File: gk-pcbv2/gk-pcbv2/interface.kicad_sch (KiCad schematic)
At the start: 69 parts, among them J11 Conn_01x02, J7 Conn_01x02, Q1 MMBT3904, Q2 MMBT3904, SW3 RotaryEncoder_Switch, SW4 SW_DIP_x01, U9 LSM6DSL

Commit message: more pcb changes
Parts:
- added J13: Conn_01x02, Connector_PinHeader_2.54mm:PinHeader_1x02_P2.54mm_Vertical, symbol Connector_Generic:Conn_01x02
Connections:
- net I2C4_SCL: now also J13.2 (Pin_2)
- net I2C4_SDA: now also J13.1 (Pin_1)

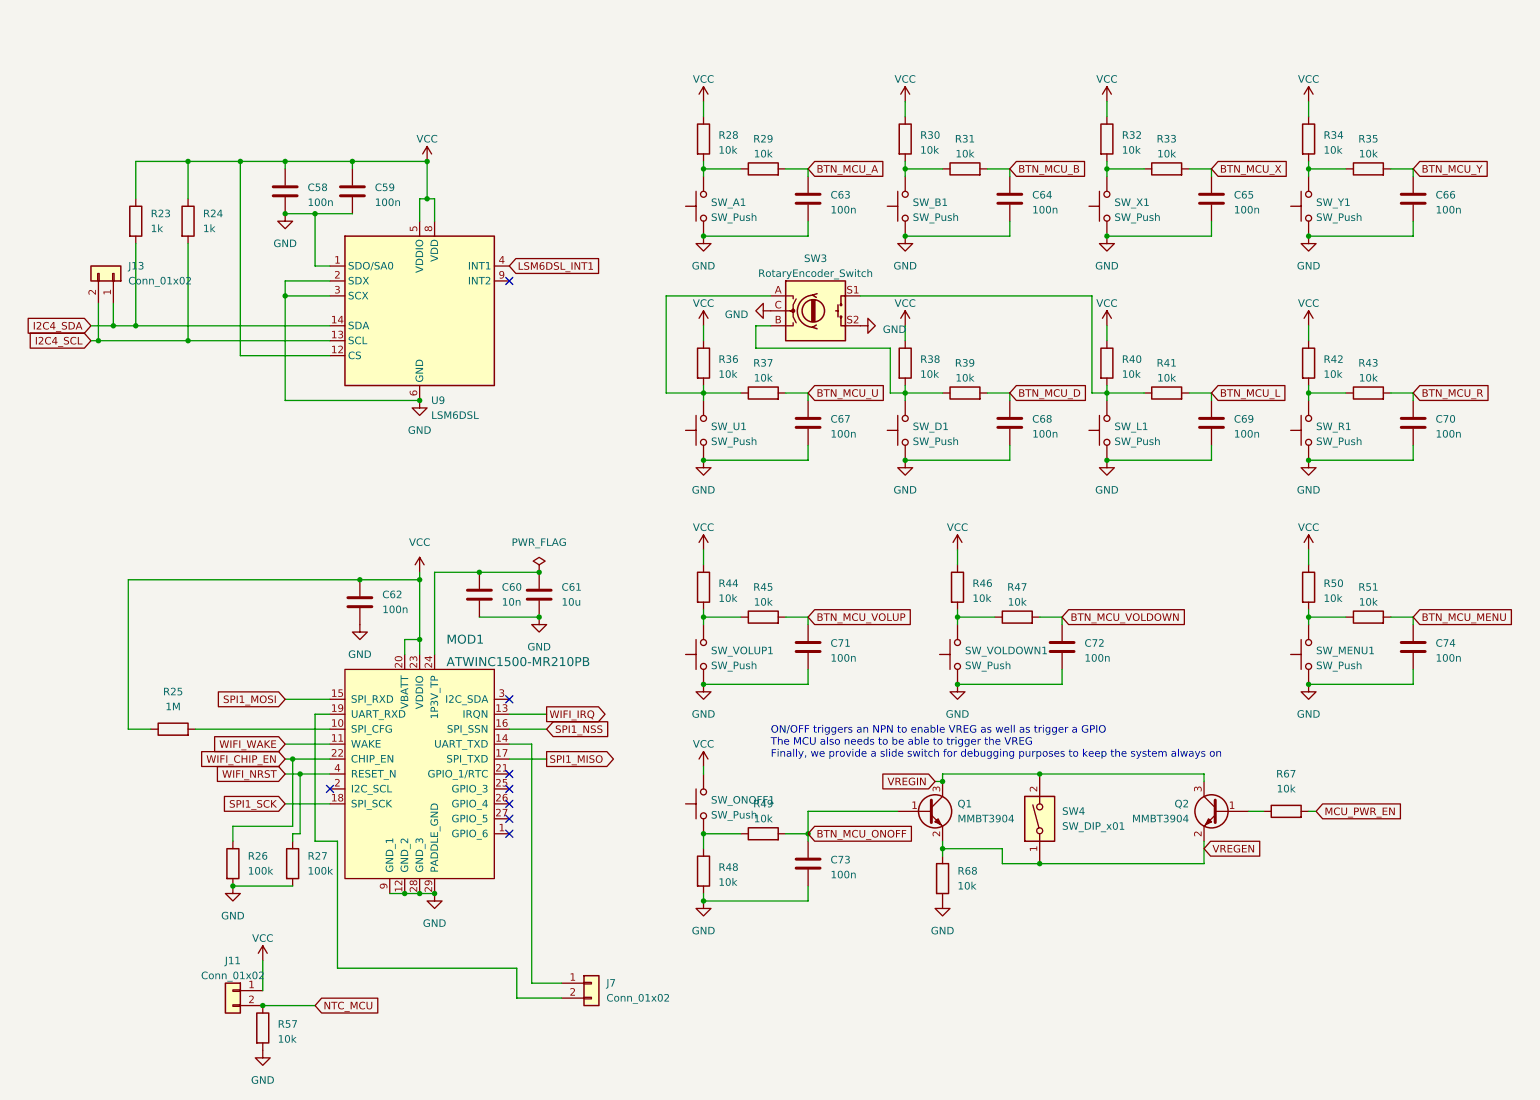
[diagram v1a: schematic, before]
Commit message: PCB updates - add xbox joystick
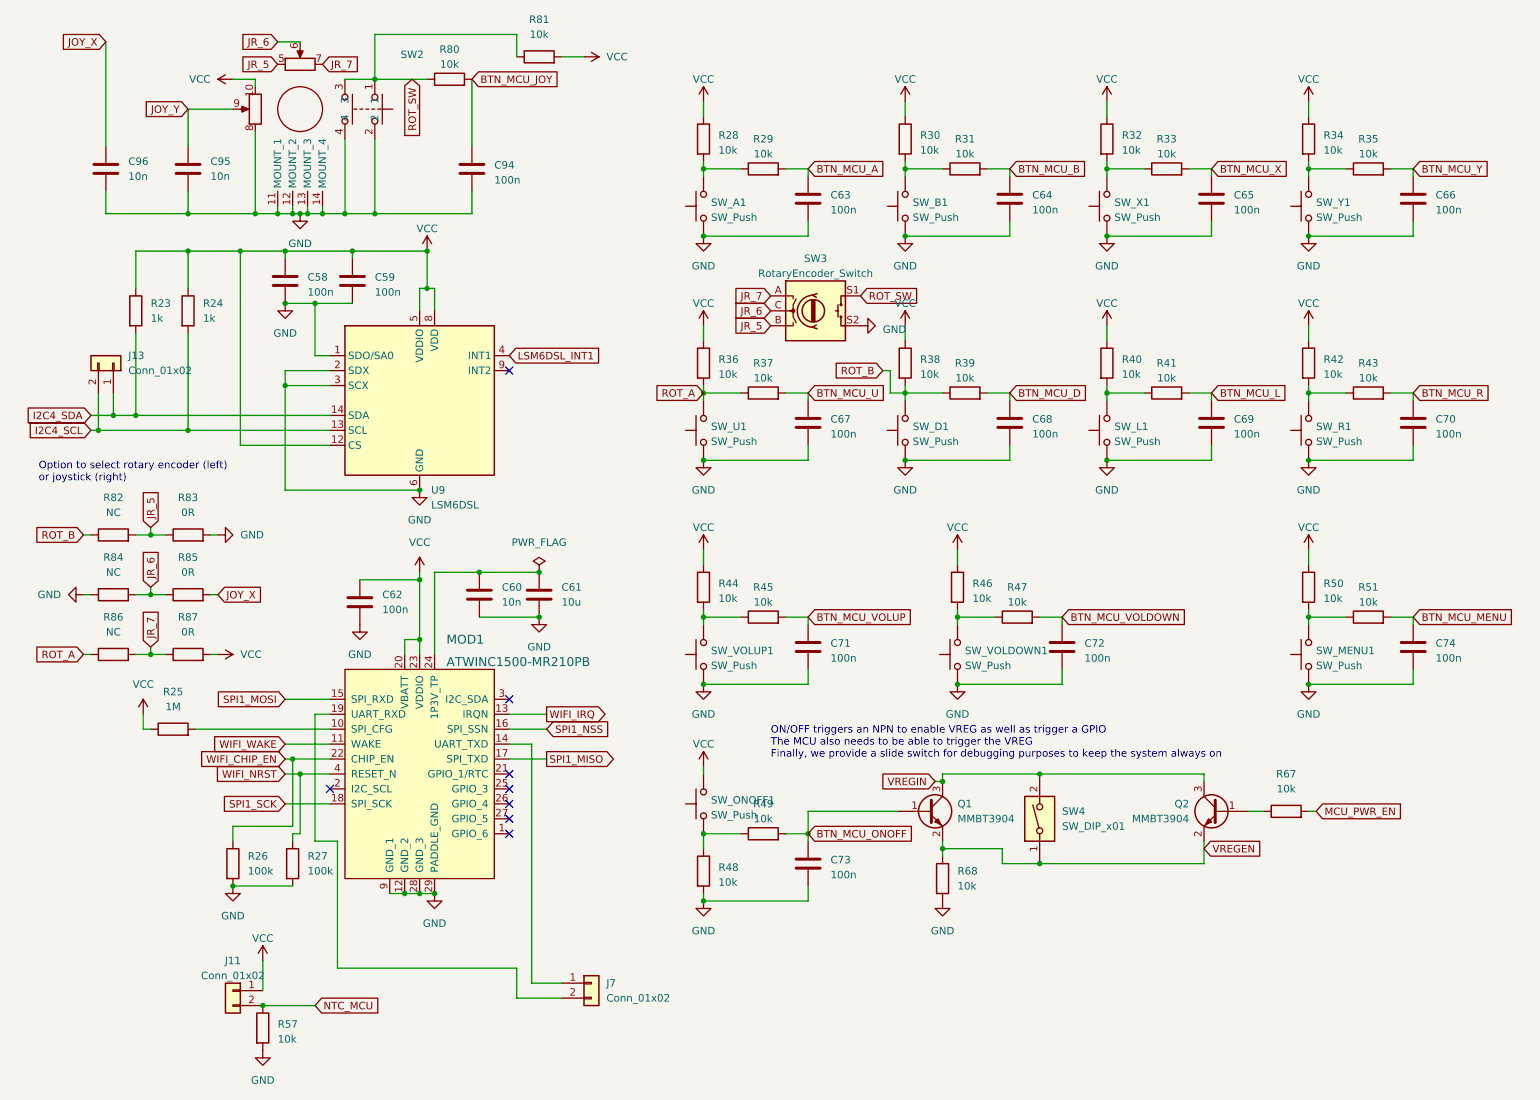
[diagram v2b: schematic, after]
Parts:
- added C94: 100n, Capacitor_SMD:C_0603_1608Metric, symbol Device:C
- added C95, C96: 10n, Capacitor_SMD:C_0603_1608Metric, symbol Device:C
- added R80, R81: 10k, Resistor_SMD:R_0603_1608Metric, symbol Device:R
- added R82, R84, R86: NC, Resistor_SMD:R_0603_1608Metric, symbol Device:R
- added R83, R85, R87: 0R, Resistor_SMD:R_0603_1608Metric, symbol Device:R
- added SW2: ~, gk:XBOX_THUMB_ROT_OVERLAP, symbol gk-syms:XBOX_THUMB
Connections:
- net GND: now also C94.2, C95.2, C96.2, R83.2, R84.1, SW2.11 (MOUNT_1), SW2.12 (MOUNT_2), SW2.13 (MOUNT_3), SW2.14 (MOUNT_4), SW2.2, SW2.4, SW2.8; no longer SW3.C
- net VCC: now also R81.2, R87.2, SW2.10
- net ROT_A: now reaches R36.2, R37.1, SW_U1.2
- net ROT_A: now also R86.1; no longer SW3.A
- net ROT_B: now reaches R38.2, R39.1, SW_D1.2
- net ROT_B: now also R82.1; no longer SW3.B
- net at R40.2, R41.1, SW_L1.2: no longer SW3.S1
- new net BTN_MCU_JOY: C94.1, R80.2
- new net JOY_X: C96.1, R85.2
- new net JOY_Y: C95.1, SW2.9
- new net JR_5: R82.2, R83.1, SW2.5, SW3.B
- new net JR_6: R84.2, R85.1, SW2.6, SW3.C
- new net JR_7: R86.2, R87.1, SW2.7, SW3.A
- new net ROT_SW: R80.1, R81.1, SW2.1, SW2.3, SW3.S1
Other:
- note added: "Option to select rotary encoder (left) or joystick (right)"
- moved on the sheet: C58, C59, J13, R23, R24, U9
